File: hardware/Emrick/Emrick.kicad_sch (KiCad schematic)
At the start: 85 parts, among them J1 LED_STRIP_CONNECTOR, J2 UFL, J3 Conn_02x05_Odd_Even, J4 BATT_CONN, P1 USB_C_Plug_USB2.0, Q1 Q_NPN_DGS, Q2 Q_NPN_DGS, Q3 Q_NPN_DGS, SW1 SW_MEC_5E (RESET), SW2 SW_SPST, U1 CC1310F128RGZR, U2 MX25R8035FZUIL0, U3 74HCT541, U4 TPS63020DSJR, U5 BQ24072RGTR, U6 CP2102N-A02-GQFN28, Y1 24MHz, Y2 32.768kHz

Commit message: update schematic and pcb
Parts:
- L1: value MHCI06030-1R5M-R8 -> 1.5uH; footprint power_inductor:IND-SMD_L7.3-W6.6 -> Inductor_SMD:L_Sunlord_MWSA0518_5.4x5.2mm
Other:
- note removed: "Consider switching this out with VDDS that will be powered by the power regulator (for operation independent of the battery)"
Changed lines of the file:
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@@
     (effects (font (size 1.27 1.27)) (justify left bottom))
   )
-  (text "Consider switching this out with VDDS \nthat will be powered by the power regulator \n(for operation independent of the battery)"
-    (at 35.56 213.36 0)
-    (effects (font (size 1.27 1.27)) (justify left bottom))
-  )
   (text "LED Strip Connection/Level Shifter" (at 16.51 132.08 0)
     (effects (font (size 2 2)) (justify left bottom))
@@
     (in_bom yes) (on_board yes)
     (property "Reference" "L1" (id 0) (at 71.12 214.63 90))
-    (property "Value" "MHCI06030-1R5M-R8" (id 1) (at 71.12 217.17 90))
-    (property "Footprint" "power_inductor:IND-SMD_L7.3-W6.6" (id 2) (at 71.12 219.71 0)
+    (property "Value" "1.5uH" (id 1) (at 71.12 217.17 90))
+    (property "Footprint" "Inductor_SMD:L_Sunlord_MWSA0518_5.4x5.2mm" (id 2) (at 71.12 219.71 0)
       (effects (font (size 1.27 1.27)) hide)
     )
@@
     )
     (path "/31746688-5aac-4a84-b28c-7b597062dcdb"
-      (reference "L1") (unit 1) (value "MHCI06030-1R5M-R8") (footprint "power_inductor:IND-SMD_L7.3-W6.6")
+      (reference "L1") (unit 1) (value "1.5uH") (footprint "Inductor_SMD:L_Sunlord_MWSA0518_5.4x5.2mm")
     )
     (path "/de1aeabd-b343-4138-8d74-7c7a871e8d81"

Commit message: Placement changes to the PCB and schematic
some footprint updates too because I realized they didn't have them in the right size
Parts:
- C24, C29, C5, C6: footprint Capacitor_SMD:C_0402_1005Metric -> Capacitor_SMD:C_0603_1608Metric
- FB1: footprint Resistor_SMD:R_0402_1005Metric -> Resistor_SMD:R_0603_1608Metric
- L7: footprint Inductor_SMD:L_0402_1005Metric -> Inductor_SMD:L_TDK_NLV32_3.2x2.5mm
- R20: value R -> 10k
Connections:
- net WMCU_VDD is gone; now on net WMCU_VDDS: R1.1, R2.1
- net GND: now also C5.1; no longer C5.2
- net BBReg_out renamed BBReg_5V
- net BBReg_5V: now also C5.2; no longer C5.1
- no-connect marks 24 -> 47
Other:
- note added: "LED Strip Connector"
- note added: "UFL connector as backup. Desolder C20 if not in use."
- note added: "VDDR Decoupling Capacitors"
- note added: "VDDS Decoupling Capacitors"
- note removed: "Decoupling Capacitors"
- note removed: "Description Needed"
- note removed: "Put LXX and CXX close to pin 33"
- note removed: "UFL connector as backup. Cut the trace of the path not being used for best results"
- title: (none) -> Project Emrick Light Strip
- moved on the sheet: AE1, C1, C10, C11, C12, C13, C14, C15, C16, C17, C18, C19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

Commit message: closer to finished placement
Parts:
- added D4: SP0503BAHT, Package_TO_SOT_SMD:SOT-143, symbol Power_Protection:SP0503BAHT
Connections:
- net GND: now also D4.1 (A)
- net USB_DMINUS: now also D4.3 (K)
- net USB_DPLUS: now also D4.4 (K)
- net VBUS: now also D4.2 (K)
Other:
- moved on the sheet: L1, R13

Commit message: route power signals on pcb
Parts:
- added R3: R, Resistor_SMD:R_0402_1005Metric, symbol Device:R
- renumbered C23 to C1, C9 to C10, C14 to C11, C20 to C12, C33 to C13, C34 to C14, C10 to C15, C22 to C16, C26 to C17, C16 to C18, C18 to C19, C25 to C2, C19 to C20, C12 to C22, C15 to C23, C32 to C24, C1 to C25, C2 to C26, C5 to C27, C6 to C28, C7 to C29, C27 to C3, C4 to C30, C11 to C31, C3 to C32, C13 to C33, C17 to C34, C29 to C4, C31 to C5, C24 to C6, C28 to C7, C30 to C8, C8 to C9, L7 to L1, L4 to L2, L2 to L3, L5 to L4, L6 to L5, L8 to L6, L3 to L7, L1 to L8, R3 to R1, R4 to R10, R6 to R11, R5 to R12, R2 to R13, R19 to R14, R17 to R15, R20 to R16, R15 to R17, R10 to R18, R18 to R19, R7 to R2, R16 to R20, R1 to R21, R11 to R4, R12 to R5, R13 to R6, R8 to R7, R9 to R8, R14 to R9, SW2 to SW1, SW1 to SW2, U3 to U1, U1 to U2, U4 to U3, U6 to U4, U2 to U5, U5 to U6
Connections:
- net WMCU_VDDS: now also R3.1; no longer J3.1 (Pin_1)
- new net: J3.1 (Pin_1), R3.2

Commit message: finish first pass at pcb
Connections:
- net BAT_CHG: now also U2.37 (DIO_24); no longer U2.17 (DIO_11)
- net BAT_PGOOD: now also U2.42 (DIO_29); no longer U2.18 (DIO_12)
- net BOOTLOADER_BACKDOOR: now also U2.19 (DIO_13); no longer U2.32 (DIO_22)
- net PWR_LED: now also U2.12 (DIO_7); no longer U2.43 (DIO_30)
- net RS485: now also U2.20 (DIO_14); no longer U2.37 (DIO_24)
- no-connect marks 47 -> 45
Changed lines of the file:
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@@
   (no_connect (at 191.77 184.15))
   (no_connect (at 217.17 38.1))
-  (no_connect (at 217.17 53.34))
-  (no_connect (at 217.17 68.58))
-  (no_connect (at 217.17 71.12))
+  (no_connect (at 217.17 91.44))
   (no_connect (at 217.17 48.26))
   (no_connect (at 217.17 50.8))
@@
   (no_connect (at 45.72 172.72))
   (no_connect (at 217.17 106.68))
-  (no_connect (at 217.17 109.22))
   (no_connect (at 217.17 88.9))
   (no_connect (at 217.17 104.14))
@@
   (no_connect (at 217.17 83.82))
   (no_connect (at 43.18 135.89))
+  (no_connect (at 217.17 111.76))
   (no_connect (at 62.23 38.1))
   (no_connect (at 62.23 43.18))
@@
     )
   )
-  (global_label "RS485" (shape input) (at 217.17 96.52 0) (fields_autoplaced)
-    (effects (font (size 1.27 1.27)) (justify left))
-    (property "Intersheet References" "${INTERSHEET_REFS}" (id 0) (at 225.6912 96.4406 0)
+  (global_label "RS485" (shape input) (at 217.17 71.12 0) (fields_autoplaced)
+    (effects (font (size 1.27 1.27)) (justify left))
+    (property "Intersheet References" "${INTERSHEET_REFS}" (id 0) (at 225.6912 71.0406 0)
       (effects (font (size 1.27 1.27)) (justify left) hide)
     )
@@
     )
   )
-  (global_label "BOOTLOADER_BACKDOOR" (shape input) (at 217.17 91.44 0) (fields_autoplaced)
-    (effects (font (size 1.27 1.27)) (justify left))
-    (property "Intersheet References" "${INTERSHEET_REFS}" (id 0) (at 242.685 91.3606 0)
+  (global_label "BOOTLOADER_BACKDOOR" (shape input) (at 217.17 68.58 0) (fields_autoplaced)
+    (effects (font (size 1.27 1.27)) (justify left))
+    (property "Intersheet References" "${INTERSHEET_REFS}" (id 0) (at 242.685 68.5006 0)
       (effects (font (size 1.27 1.27)) (justify left) hide)
     )
@@
     )
   )
-  (global_label "PWR_LED" (shape input) (at 217.17 111.76 0) (fields_autoplaced)
-    (effects (font (size 1.27 1.27)) (justify left))
-    (property "Intersheet References" "${INTERSHEET_REFS}" (id 0) (at 227.9893 111.6806 0)
+  (global_label "PWR_LED" (shape input) (at 217.17 53.34 0) (fields_autoplaced)
+    (effects (font (size 1.27 1.27)) (justify left))
+    (property "Intersheet References" "${INTERSHEET_REFS}" (id 0) (at 227.9893 53.2606 0)
       (effects (font (size 1.27 1.27)) (justify left) hide)
     )
@@
     )
   )
-  (global_label "BAT_PGOOD" (shape input) (at 217.17 66.04 0) (fields_autoplaced)
-    (effects (font (size 1.27 1.27)) (justify left))
-    (property "Intersheet References" "${INTERSHEET_REFS}" (id 0) (at 230.3479 65.9606 0)
+  (global_label "BAT_PGOOD" (shape input) (at 217.17 109.22 0) (fields_autoplaced)
+    (effects (font (size 1.27 1.27)) (justify left))
+    (property "Intersheet References" "${INTERSHEET_REFS}" (id 0) (at 230.3479 109.1406 0)
       (effects (font (size 1.27 1.27)) (justify left) hide)
     )
@@
     )
   )
-  (global_label "BAT_CHG" (shape input) (at 217.17 63.5 0) (fields_autoplaced)
-    (effects (font (size 1.27 1.27)) (justify left))
-    (property "Intersheet References" "${INTERSHEET_REFS}" (id 0) (at 227.7474 63.4206 0)
-      (effects (font (size 1.27 1.27)) (justify left) hide)
-    )
+  (global_label "BAT_CHG" (shape input) (at 217.17 96.52 0) (fields_autoplaced)
+    (effects (font (size 1.27 1.27)) (justify left))
+    (property "Intersheet References" "${INTERSHEET_REFS}" (id 0) (at 227.7474 96.4406 0)
+      (effects (font (size 1.27 1.27)) (justify left) hide)
+    )

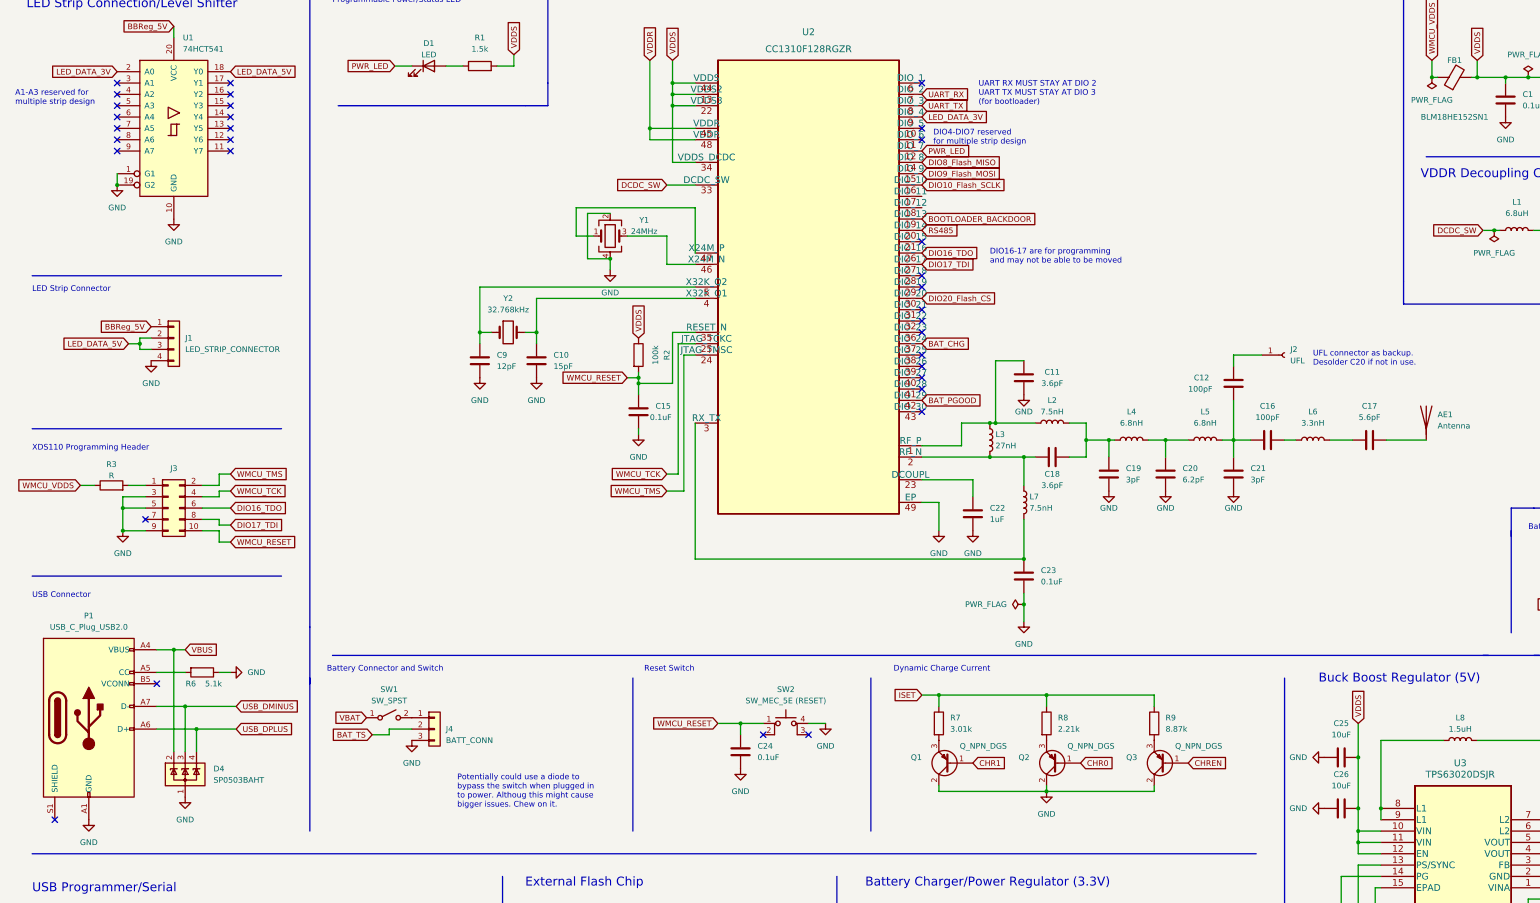
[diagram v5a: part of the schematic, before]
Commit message: update pcb and schematic and add antenna development kit
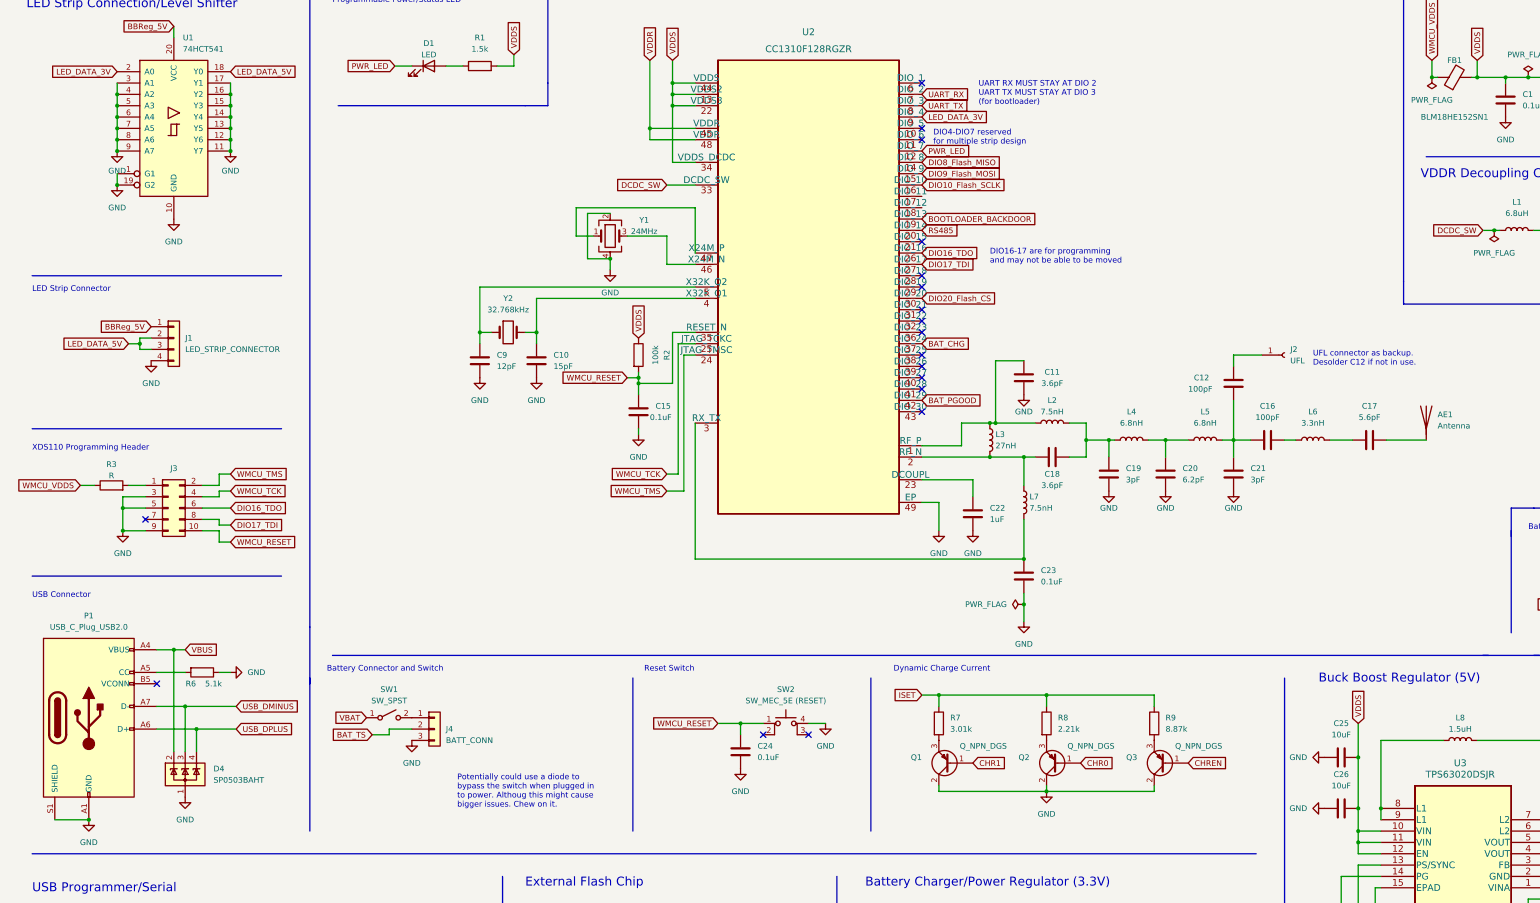
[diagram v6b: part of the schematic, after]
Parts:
- R7, R8, R9: footprint Resistor_SMD:R_0402_1005Metric -> Resistor_SMD:R_0603_1608Metric
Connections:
- net GND: now also P1.S1 (SHIELD), U1.11 (Y7), U1.12 (Y6), U1.13 (Y5), U1.14 (Y4), U1.15 (Y3), U1.16 (Y2), U1.17 (Y1), U1.3 (A1), U1.4 (A2), U1.5 (A3), U1.6 (A4), U1.7 (A5), U1.8 (A6), U1.9 (A7)
- no-connect marks 45 -> 30
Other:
- note added: "UFL connector as backup. Desolder C12 if not in use."
- note removed: "A1-A3 reserved for multiple strip design"
- note removed: "UFL connector as backup. Desolder C20 if not in use."

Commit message: added pullup to reset circuitry
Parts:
- added R?: 100k, symbol Device:R
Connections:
- net BBReg_5V: no longer U1.20 (VCC)
- net GND: now also U1.2 (A0); no longer U1.1 (G1), U1.10 (GND), U1.11 (Y7), U1.12 (Y6), U1.13 (Y5), U1.14 (Y4), U1.15 (Y3), U1.16 (Y2), U1.17 (Y1), U1.19 (G2), U1.3 (A1), U1.4 (A2), U1.5 (A3), U1.6 (A4), U1.7 (A5), U1.8 (A6), U1.9 (A7)
- net LED_DATA_3V: now also U1.18 (Y0); no longer U1.2 (A0)
- net LED_DATA_5V: no longer U1.18 (Y0)
- net VDDS: now also R?.1
- net WMCU_RESET: now also R?.2
- no-connect marks 30 -> 37
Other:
- moved on the sheet: U1

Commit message: Revert "added pullup to reset circuitry"
This reverts commit 352271496a808d8b1eb14a86bebbd64d10ea0814.
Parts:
- removed R?: 100k, symbol Device:R
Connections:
- net BBReg_5V: now also U1.20 (VCC)
- net GND: now also U1.1 (G1), U1.10 (GND), U1.11 (Y7), U1.12 (Y6), U1.13 (Y5), U1.14 (Y4), U1.15 (Y3), U1.16 (Y2), U1.17 (Y1), U1.19 (G2), U1.3 (A1), U1.4 (A2), U1.5 (A3), U1.6 (A4), U1.7 (A5), U1.8 (A6), U1.9 (A7); no longer U1.2 (A0)
- net LED_DATA_3V: now also U1.2 (A0); no longer U1.18 (Y0)
- net LED_DATA_5V: now also U1.18 (Y0)
- no-connect marks 37 -> 30
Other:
- moved on the sheet: U1
